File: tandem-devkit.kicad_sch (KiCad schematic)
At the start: 25 parts, among them J101 Conn_01x03, J102 Conn_01x03, J103 Conn_01x06, J104 Conn_01x04, J105 Conn_01x02, J106 QWIIC I2C Connector

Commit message: Ficup column name for JLCPCB/LCSC part no
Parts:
- J105: LCSC (none) -> C173752
- J106: LCSC (none) -> C145956
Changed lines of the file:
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@@
+      (effects (font (size 1.27 1.27)) hide)
+    )
+    (property "LCSC" "C145956" (id 5) (at 213.36 133.35 0)
       (effects (font (size 1.27 1.27)) hide)
     )
@@
       (effects (font (size 1.27 1.27)) hide)
     )
+    (property "LCSC" " C173752 " (id 5) (at 153.035 127 0)
+      (effects (font (size 1.27 1.27)) hide)
+    )

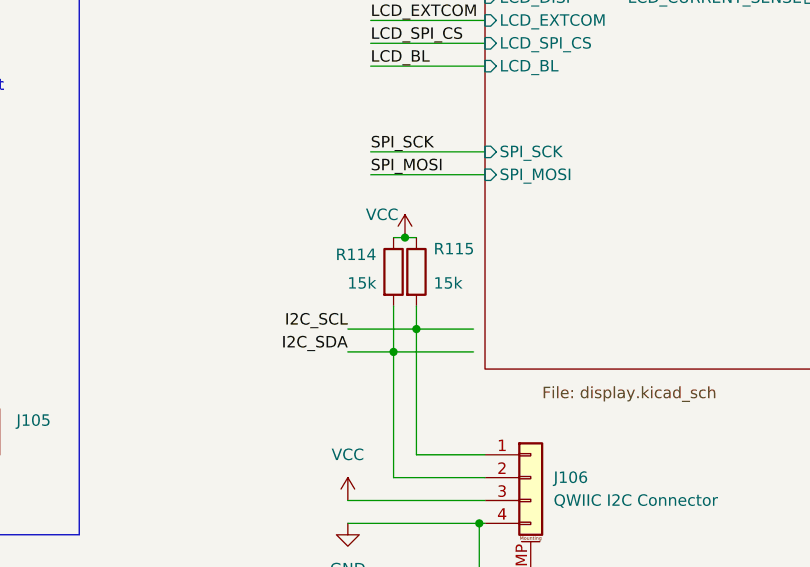
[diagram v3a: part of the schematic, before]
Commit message: schematic: change i2c pull-ups to 2k2
As mentioned as "Phil's Lab" mentions as his suggested value
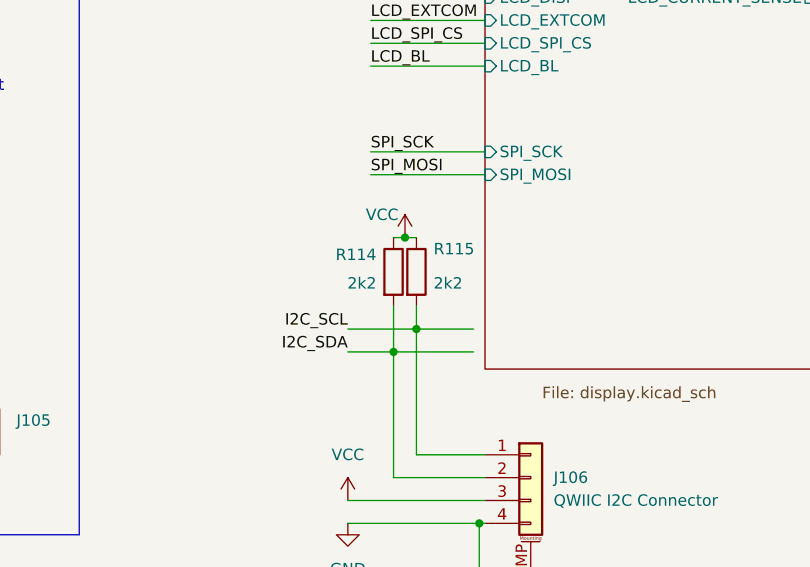
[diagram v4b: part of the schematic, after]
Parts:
- R114, R115: value 15k -> 2k2
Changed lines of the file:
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@@
       (effects (font (size 1.27 1.27)) (justify left))
     )
-    (property "Value" "15k" (id 1) (at 202.565 111.76 0)
+    (property "Value" "2k2" (id 1) (at 202.565 111.76 0)
       (effects (font (size 1.27 1.27)) (justify left))
     )
@@
       (effects (font (size 1.27 1.27)) (justify right))
     )
-    (property "Value" "15k" (id 1) (at 196.215 111.76 0)
+    (property "Value" "2k2" (id 1) (at 196.215 111.76 0)
       (effects (font (size 1.27 1.27)) (justify right))
     )
@@
     )
     (path "/e81fd5ee-84b2-46cd-8a31-6bfa0b10fff7"
-      (reference "R114") (unit 1) (value "15k") (footprint "Resistor_SMD:R_0603_1608Metric")
+      (reference "R114") (unit 1) (value "2k2") (footprint "Resistor_SMD:R_0603_1608Metric")
     )
     (path "/846991a6-26d3-4f19-93e3-371850340145"
-      (reference "R115") (unit 1) (value "15k") (footprint "Resistor_SMD:R_0603_1608Metric")
+      (reference "R115") (unit 1) (value "2k2") (footprint "Resistor_SMD:R_0603_1608Metric")
     )
     (path "/d5fdcc1b-217f-4399-86f5-956578dadb93/1bda3ed1-0820-41a7-aa64-a117b5c741ee"

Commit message: Mark some parts as 'exclude from bom'
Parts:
- A101, A102, J101, J102, J103, J104, TP101, TP102: now left out of the parts list
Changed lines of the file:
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@@
   )
   (symbol (lib_id "project-lib:Adafruit_ItsyBitsi_nrf5240-pins-passive") (at 60.96 93.98 0) (unit 1)
-    (in_bom yes) (on_board yes)
+    (in_bom no) (on_board yes)
     (property "Reference" "A101" (id 0) (at 50.8 62.865 0)
       (effects (font (size 1.27 1.27)) (justify left))
@@
   )
   (symbol (lib_id "Connector_Generic:Conn_01x01") (at 251.46 151.13 0) (unit 1)
-    (in_bom yes) (on_board yes) (fields_autoplaced)
+    (in_bom no) (on_board yes) (fields_autoplaced)
     (property "Reference" "TP102" (id 0) (at 254 149.8599 0)
       (effects (font (size 1.27 1.27)) (justify left))
@@
   )
   (symbol (lib_name "Conn_01x03_2") (lib_id "Connector_Generic:Conn_01x03") (at 59.055 152.4 90) (unit 1)
-    (in_bom yes) (on_board yes) (fields_autoplaced)
+    (in_bom no) (on_board yes) (fields_autoplaced)
     (property "Reference" "J102" (id 0) (at 64.77 151.1299 90)
       (effects (font (size 1.27 1.27)) (justify right) hide)
@@
   )
   (symbol (lib_id "project-lib:Adafruit_Feather_nrf52840") (at 60.96 93.98 0) (unit 1)
-    (in_bom yes) (on_board yes)
+    (in_bom no) (on_board yes)
     (property "Reference" "A102" (id 0) (at 50.8 64.77 0)
       (effects (font (size 1.27 1.27)) (justify left))
@@
   )
   (symbol (lib_name "Conn_01x03_1") (lib_id "Connector_Generic:Conn_01x03") (at 50.165 152.4 90) (unit 1)
-    (in_bom yes) (on_board yes) (fields_autoplaced)
+    (in_bom no) (on_board yes) (fields_autoplaced)
     (property "Reference" "J101" (id 0) (at 55.88 151.1299 90)
       (effects (font (size 1.27 1.27)) (justify right) hide)
@@
   )
   (symbol (lib_id "Connector_Generic:Conn_01x03") (at 213.36 153.67 0) (unit 1)
-    (in_bom yes) (on_board yes)
+    (in_bom no) (on_board yes)
     (property "Reference" "TP101" (id 0) (at 208.915 147.32 0)
       (effects (font (size 1.27 1.27)) (justify left))
@@
   )
   (symbol (lib_id "Connector_Generic:Conn_01x04") (at 84.455 152.4 90) (unit 1)
-    (in_bom yes) (on_board yes) (fields_autoplaced)
+    (in_bom no) (on_board yes) (fields_autoplaced)
     (property "Reference" "J104" (id 0) (at 85.725 146.05 90)
       (effects (font (size 1.27 1.27)) hide)
@@
   )
   (symbol (lib_id "Connector_Generic:Conn_01x06") (at 70.485 152.4 90) (unit 1)
-    (in_bom yes) (on_board yes) (fields_autoplaced)
+    (in_bom no) (on_board yes) (fields_autoplaced)
     (property "Reference" "J103" (id 0) (at 76.2 151.1299 90)
       (effects (font (size 1.27 1.27)) (justify right) hide)
@@
     )
     (path "/d5fdcc1b-217f-4399-86f5-956578dadb93/c53873f5-9695-4025-af4f-ae2b36f12765"
-      (reference "TP201") (unit 1) (value "TestPoint_2Pole") (footprint "project-lib:TestPoint_1x03_P1.27mm")
+      (reference "TP201") (unit 1) (value "TestPoint_3Pole") (footprint "project-lib:TestPoint_1x03_P1.27mm")
     )
     (path "/d5fdcc1b-217f-4399-86f5-956578dadb93/a2fb0544-d95c-41d8-b9d9-9e6f40daef54"
-      (reference "TP202") (unit 1) (value "TestPoint_2Pole") (footprint "project-lib:TestPoint_1x03_P1.27mm")
+      (reference "TP202") (unit 1) (value "TestPoint_3Pole") (footprint "project-lib:TestPoint_1x03_P1.27mm")
     )
     (path "/af27d833-7492-473b-b609-10c30f242124/2b371f37-1eb1-4232-a254-abe936f288d8"
-      (reference "TP301") (unit 1) (value "TestPoint_2Pole") (footprint "project-lib:TestPoint_1x03_P1.27mm")
+      (reference "TP301") (unit 1) (value "TestPoint_3Pole") (footprint "project-lib:TestPoint_1x03_P1.27mm")
     )
     (path "/af27d833-7492-473b-b609-10c30f242124/b7667ad9-97b9-47de-ad1e-8981ef445695"
-      (reference "TP302") (unit 1) (value "TestPoint_2Pole") (footprint "project-lib:TestPoint_1x03_P1.27mm")
+      (reference "TP302") (unit 1) (value "TestPoint_3Pole") (footprint "project-lib:TestPoint_1x03_P1.27mm")
     )
     (path "/d5fdcc1b-217f-4399-86f5-956578dadb93/5f930c8e-d5bc-48a4-9115-3a9dfe4e2330"

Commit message: Schematic: BOM consolidation and JLCPCB part no annotation
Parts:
- J105: LCSC C173752 -> C173752
- R101, R102, R103, R104, R105, R106, R107, R108, R109, R110, R111, R112, R113: LCSC (none) -> C23345
- R114, R115: LCSC (none) -> C4190
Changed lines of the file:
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@@
+      (effects (font (size 1.27 1.27)) hide)
+    )
+    (property "LCSC" "C23345" (id 4) (at 40.005 96.52 0)
       (effects (font (size 1.27 1.27)) hide)
     )
@@
       (effects (font (size 1.27 1.27)) hide)
     )
+    (property "LCSC" "C23345" (id 4) (at 40.005 91.44 0)
+      (effects (font (size 1.27 1.27)) hide)
+    )
     (pin "1")
     (pin "2")
@@
       (effects (font (size 1.27 1.27)) hide)
     )
+    (property "LCSC" "C23345" (id 4) (at 40.005 76.2 0)
+      (effects (font (size 1.27 1.27)) hide)
+    )
     (pin "1")
     (pin "2")
@@
       (effects (font (size 1.27 1.27)) hide)
     )
+    (property "LCSC" "C23345" (id 4) (at 40.005 81.28 0)
+      (effects (font (size 1.27 1.27)) hide)
+    )
     (pin "1")
     (pin "2")
@@
       (effects (font (size 1.27 1.27)) hide)
     )
+    (property "LCSC" "C23345" (id 4) (at 40.005 106.68 0)
+      (effects (font (size 1.27 1.27)) hide)
+    )
     (pin "1")
     (pin "2")
@@
       (effects (font (size 1.27 1.27)) hide)
     )
+    (property "LCSC" "C23345" (id 4) (at 40.005 83.82 0)
+      (effects (font (size 1.27 1.27)) hide)
+    )
     (pin "1")
     (pin "2")
@@
     )
     (property "Datasheet" "~" (id 3) (at 40.005 99.06 0)
+      (effects (font (size 1.27 1.27)) hide)
+    )
+    (property "LCSC" "C23345" (id 4) (at 40.005 99.06 0)
       (effects (font (size 1.27 1.27)) hide)
     )
@@
       (effects (font (size 1.27 1.27)) hide)
     )
+    (property "LCSC" "C23345" (id 4) (at 40.005 116.84 0)
+      (effects (font (size 1.27 1.27)) hide)
+    )
     (pin "1")
     (pin "2")
@@
       (effects (font (size 1.27 1.27)) hide)
     )
+    (property "LCSC" "C23345" (id 4) (at 40.005 109.22 0)
+      (effects (font (size 1.27 1.27)) hide)
+    )
     (pin "1")
     (pin "2")
@@
     )
     (property "Datasheet" "~" (id 3) (at 200.66 110.49 0)
+      (effects (font (size 1.27 1.27)) hide)
+    )
+    (property "LCSC" "C4190" (id 4) (at 200.66 110.49 0)
       (effects (font (size 1.27 1.27)) hide)
     )
@@
       (effects (font (size 1.27 1.27)) hide)
     )
+    (property "LCSC" "C23345" (id 4) (at 40.005 114.3 0)
+      (effects (font (size 1.27 1.27)) hide)
+    )
     (pin "1")
     (pin "2")
@@
     )
     (property "Datasheet" "~" (id 3) (at 40.005 73.66 0)
+      (effects (font (size 1.27 1.27)) hide)
+    )
+    (property "LCSC" "C23345" (id 4) (at 40.005 73.66 0)
       (effects (font (size 1.27 1.27)) hide)
     )
@@
       (effects (font (size 1.27 1.27)) hide)
     )
+    (property "LCSC" "C4190" (id 4) (at 198.12 110.49 0)
+      (effects (font (size 1.27 1.27)) hide)
+    )
     (pin "1")
     (pin "2")
@@
       (effects (font (size 1.27 1.27)) hide)
     )
+    (property "LCSC" "C23345" (id 4) (at 40.005 86.36 0)
+      (effects (font (size 1.27 1.27)) hide)
+    )
     (pin "1")
     (pin "2")
@@
       (effects (font (size 1.27 1.27)) hide)
     )
-    (property "LCSC" " C173752 " (id 5) (at 153.035 127 0)
+    (property "LCSC" "C173752 " (id 5) (at 153.035 127 0)
       (effects (font (size 1.27 1.27)) hide)
     )
@@
     )
     (property "Datasheet" "~" (id 3) (at 40.005 88.9 0)
+      (effects (font (size 1.27 1.27)) hide)
+    )
+    (property "LCSC" "C23345" (id 4) (at 40.005 88.9 0)
       (effects (font (size 1.27 1.27)) hide)
     )
@@
     )
     (path "/d5fdcc1b-217f-4399-86f5-956578dadb93/891c1ce7-68b0-454f-be85-97ff9d4bfe99"
-      (reference "R204") (unit 1) (value "500m") (footprint "Resistor_SMD:R_0805_2012Metric")
+      (reference "R204") (unit 1) (value "0.5") (footprint "Resistor_SMD:R_0805_2012Metric")
     )
     (path "/d5fdcc1b-217f-4399-86f5-956578dadb93/c7c4dff9-c0af-42e1-9b10-9445f0b13ba1"
@@
     )
     (path "/d5fdcc1b-217f-4399-86f5-956578dadb93/1d226038-a34d-4c46-b825-d17f91a05383"
-      (reference "R210") (unit 1) (value "500m") (footprint "Resistor_SMD:R_0805_2012Metric")
+      (reference "R210") (unit 1) (value "0.5") (footprint "Resistor_SMD:R_0805_2012Metric")
     )
     (path "/d5fdcc1b-217f-4399-86f5-956578dadb93/3a6e8612-e1aa-47a1-9674-6cedae332e1c"
@@
     )
     (path "/af27d833-7492-473b-b609-10c30f242124/d8b92c08-91d9-4b14-80b8-8f95ca96eee3"
-      (reference "R301") (unit 1) (value "500m") (footprint "Resistor_SMD:R_0805_2012Metric")
+      (reference "R301") (unit 1) (value "0.5") (footprint "Resistor_SMD:R_0805_2012Metric")
     )
     (path "/af27d833-7492-473b-b609-10c30f242124/cfe85812-ef50-4e0c-b38b-5ad4a475d9c4"
-      (reference "R302") (unit 1) (value "500m") (footprint "Resistor_SMD:R_0805_2012Metric")
+      (reference "R302") (unit 1) (value "0.5") (footprint "Resistor_SMD:R_0805_2012Metric")
     )
     (path "/af27d833-7492-473b-b609-10c30f242124/a2ec8936-2bb0-45bb-bf7a-a099d79c6737"
@@
     )
     (path "/af27d833-7492-473b-b609-10c30f242124/bf2aae44-fb84-4a21-ac7b-79750543e3ef"
-      (reference "R307") (unit 1) (value "0.47") (footprint "Resistor_SMD:R_0603_1608Metric")
+      (reference "R307") (unit 1) (value "0.5") (footprint "Resistor_SMD:R_0805_2012Metric")
     )
     (path "/af27d833-7492-473b-b609-10c30f242124/ceb5cfa1-de0f-4f9a-9fc5-f1e5839401d9"
